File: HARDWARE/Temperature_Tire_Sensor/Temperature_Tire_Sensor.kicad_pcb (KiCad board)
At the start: 4 copper layers, 42 parts, among them IC1 MLX90621ESF-BAB-000-SP, J1 SWD_01x06, J2 CAN_01x04, SW1 RESET, U1 STM32L4P5RET6, U2 MIC5236, U3 MIC5306-2.6YD5-TR, U4 SN65HVD232, Y1 16MGHz

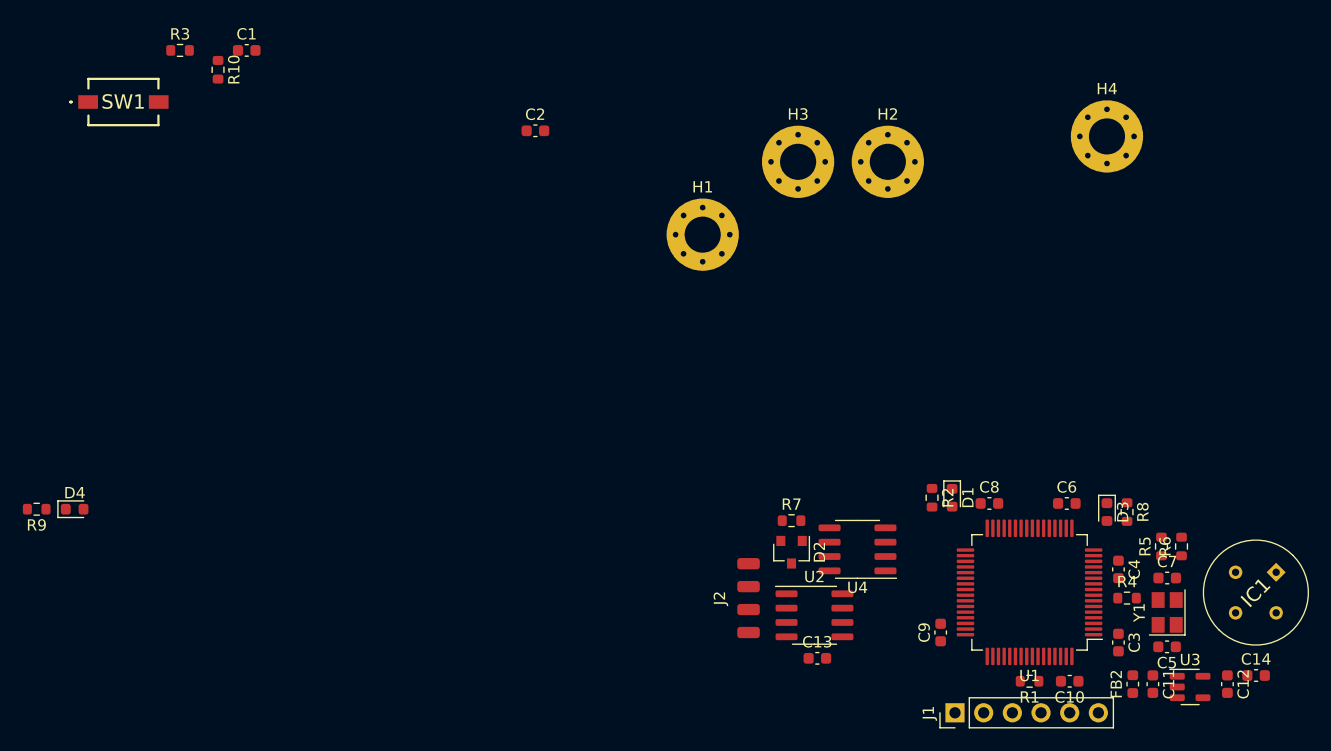
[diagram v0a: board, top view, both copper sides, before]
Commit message: pcb layout done - waiting for the confirmation of layout V1
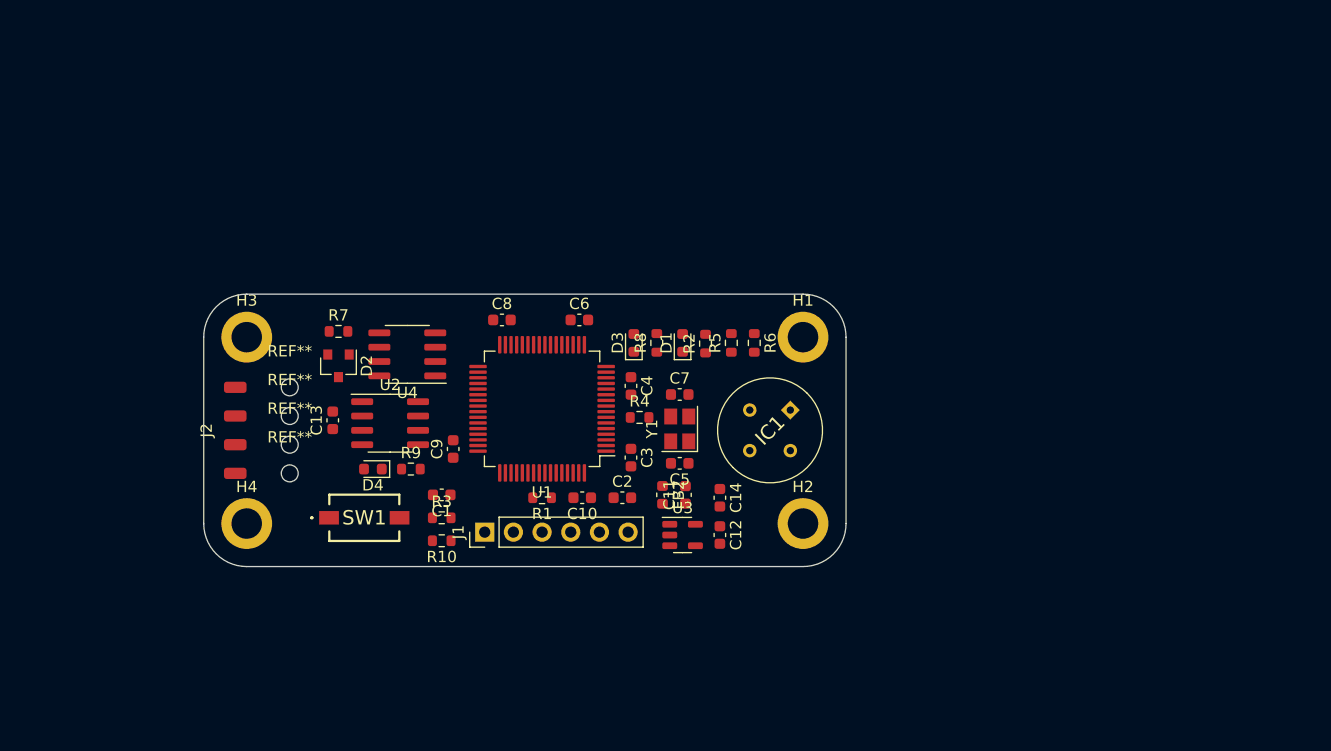
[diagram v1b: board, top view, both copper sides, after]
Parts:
- added REF**: MountingHole_2.1mm, MountingHole:MountingHole_2.1mm, F.Cu at (120.7, 111.1)
- added REF**: MountingHole_2.1mm, MountingHole:MountingHole_2.1mm, F.Cu at (120.7, 108.6)
- added REF**: MountingHole_2.1mm, MountingHole:MountingHole_2.1mm, F.Cu at (120.7, 116.2)
- added REF**: MountingHole_2.1mm, MountingHole:MountingHole_2.1mm, F.Cu at (120.7, 113.7)
- H1, H2, H3, H4: footprint MountingHole:MountingHole_3.2mm_M3_Pad_Via -> MountingHole:MountingHole_2.7mm_M2.5_ISO14580_Pad
- moved H4 83.6 mm to (116.8, 120.7)
- moved H3 51.2 mm to (116.8, 104.1)
- moved C14 50.0 mm to (158.8, 118.4), turned to -90 degrees
- moved J2 47.8 mm to (115.8, 112.4)
- moved C13 47.8 mm to (124.5, 111.5), turned to 90 degrees
- moved R3 47.4 mm to (134.1, 120.1)
- moved U3 46.9 mm to (155.4, 121.7)
- moved C12 46.9 mm to (158.8, 121.7)
- moved R10 46.2 mm to (134.1, 122.2), turned to 180 degrees
- moved C3 46.2 mm to (150.9, 114.8)
- moved C10 46.1 mm to (146.6, 118.4)
- moved C4 46.1 mm to (150.9, 108.5)
- moved C6 46.1 mm to (146.3, 102.6)
- moved C7 46.1 mm to (155.2, 109.2)
- moved C8 46.1 mm to (139.4, 102.6)
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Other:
- board outline added: 56.9 x 24.1 mm

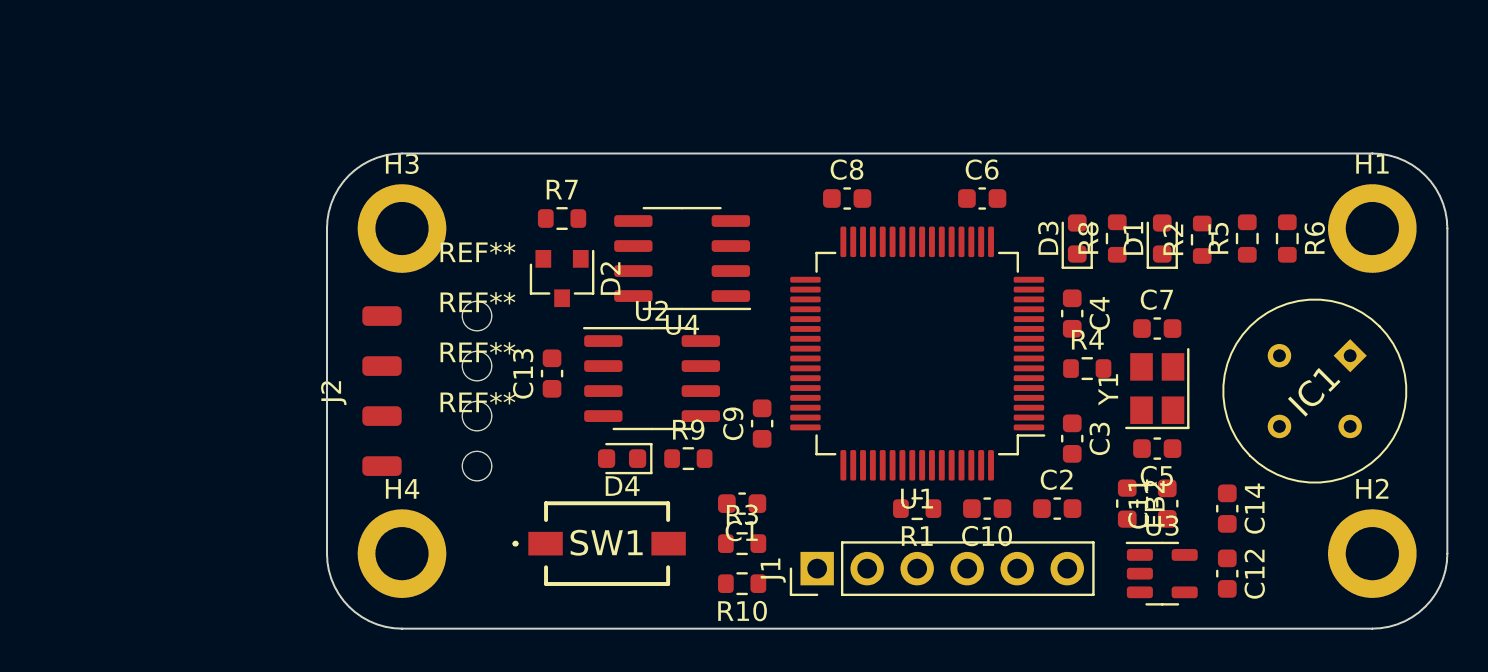
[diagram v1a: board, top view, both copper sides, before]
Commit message: Power planes has been added
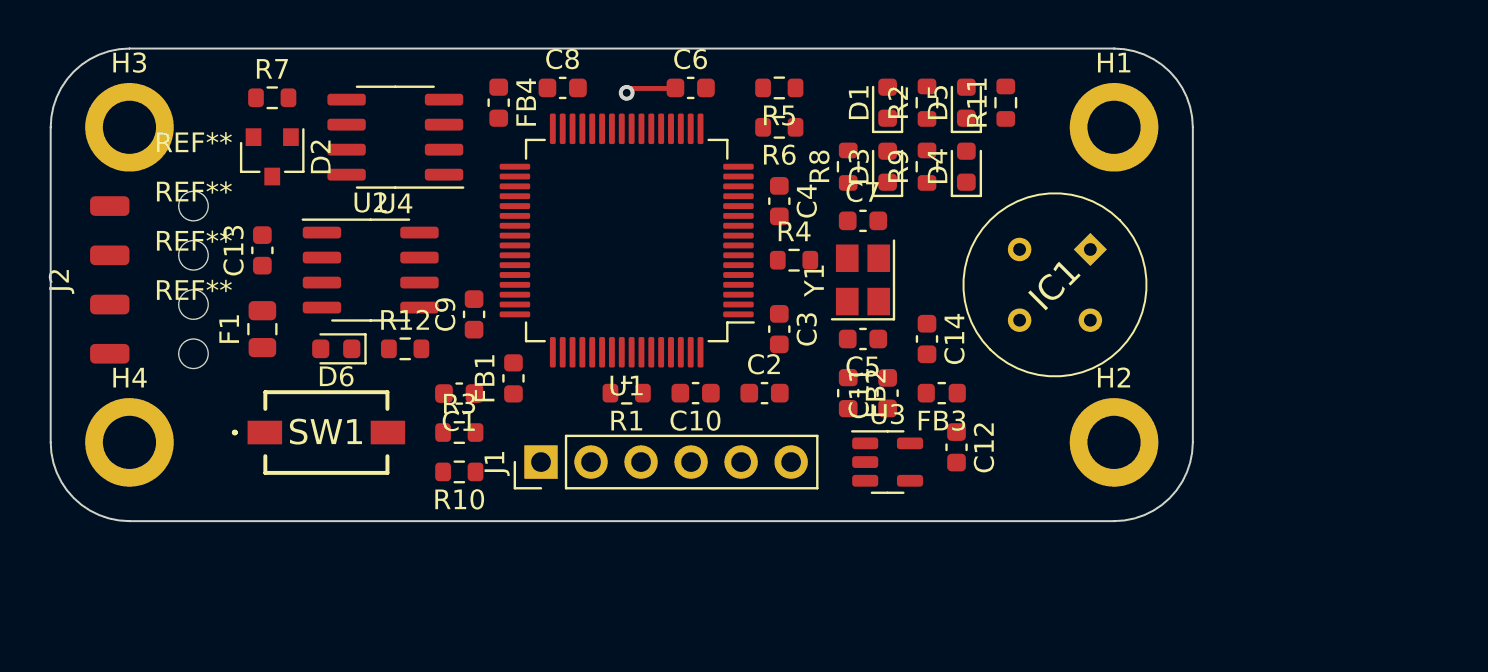
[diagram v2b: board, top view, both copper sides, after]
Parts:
- added D5: GREEN, Diode_SMD:D_0603_1608Metric, F.Cu at (145.5, 97.8)
- added D6: RED, Diode_SMD:D_0603_1608Metric, F.Cu at (113.5, 110.2)
- added F1: Polyfuse, Fuse:Fuse_0805_2012Metric, F.Cu at (109.8, 109.2)
- added FB1: 60R@100MHz, Inductor_SMD:L_0603_1608Metric, F.Cu at (122.5, 111.8)
- added FB3: 60R@100MHz, Inductor_SMD:L_0603_1608Metric, F.Cu at (144.2, 112.5)
- added FB4: 60R@100MHz, Inductor_SMD:L_0603_1608Metric, F.Cu at (121.8, 97.8)
- added R11: 1k5, Resistor_SMD:R_0603_1608Metric, F.Cu at (147.5, 97.8)
- added R12: 1k5, Resistor_SMD:R_0603_1608Metric, F.Cu at (117.0, 110.2)
- D1: value BLUE -> RED
- D3, D4: value RED -> YELLOW
- moved R6 26.4 mm to (136.0, 99.0), turned to 180 degrees
- moved R5 25.0 mm to (136.0, 97.0), turned to 180 degrees
- moved D4 22.9 mm to (145.5, 101.0), turned to 90 degrees
- moved R9 19.1 mm to (143.5, 101.0), turned to 90 degrees
- moved C14 17.5 mm to (143.5, 109.8)
- moved C13 16.0 mm to (109.8, 105.2)
- moved C2 16.0 mm to (135.2, 112.5)
- moved D2 16.0 mm to (110.2, 100.5)
- moved C5 15.9 mm to (140.2, 109.8)
- moved R7 15.9 mm to (110.2, 97.5)
- moved C4 15.9 mm to (136.0, 102.8)
- moved Y1 15.9 mm to (140.2, 106.8)
- moved C10 15.9 mm to (131.8, 112.5)
- moved C7 15.9 mm to (140.2, 103.8)
- moved C3 15.9 mm to (136.0, 109.2)
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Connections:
- C10 pad 1: +3V3 -> /+3V3_uC
- C14 pad 1: +2V6 -> Net-(C14-Pad1)
- C2 pad 1: +3V3 -> /+3V3_uC
- C3 pad 1: +3V3 -> /+3V3_uC
- C4 pad 1: +3V3 -> /+3V3_uC
- C6 pad 1: +3V3 -> /+3V3_uC
- C8 pad 1: +3V3 -> /+3V3_uC
- C9 pad 1: +3V3 -> /+3V3_uC
- D1 pad 2: /LED -> /LED_ERR
- D3 pad 2: /LED_ERR -> /LED_WAR1
- D4 pad 2: +3V3 -> /LED_WAR2
- IC1 pad 3: +2V6 -> Net-(C14-Pad1)
- U1 pad 1: +3V3 -> /+3V3_uC
- U1 pad 13: +3V3 -> /+3V3_uC
- U1 pad 16: unconnected-(U1-Pad16) -> /LED_WAR2
- U1 pad 19: +3V3 -> /+3V3_uC
- U1 pad 24: unconnected-(U1-Pad24) -> /LED_WAR1
- U1 pad 26: /LED -> /LED_OK
- U1 pad 32: +3V3 -> /+3V3_uC
- U1 pad 48: +3V3 -> /+3V3_uC
- U1 pad 64: +3V3 -> /+3V3_uC
- U2 pad 2: +24V -> Net-(F1-Pad2)
- U2 pad 4: +24V -> Net-(F1-Pad2)
- U4 pad 3: +3V3 -> Net-(FB4-Pad2)
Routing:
- net /+3V3_uC: track 0.00 -> 2.81 mm, vias 0 -> 1
- added copper zone on In2.Cu, net +3V3
- added copper zone on In2.Cu, net /+3V3_uC
- added copper zone on In1.Cu, net GND
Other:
- board size 56.9 x 24.1 mm -> 58 x 24 mm

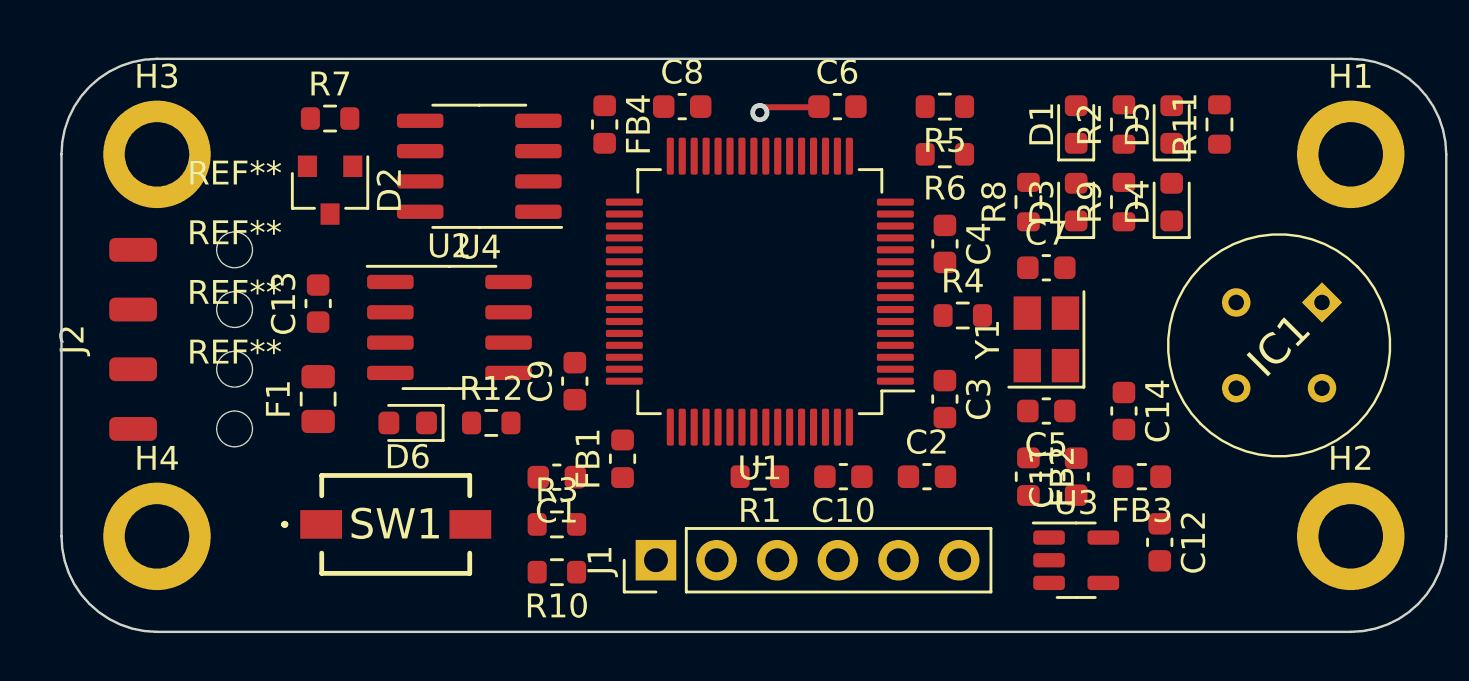
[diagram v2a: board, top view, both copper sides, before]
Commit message: Routing mostly done - GND and 3V3_uC vias have to be added
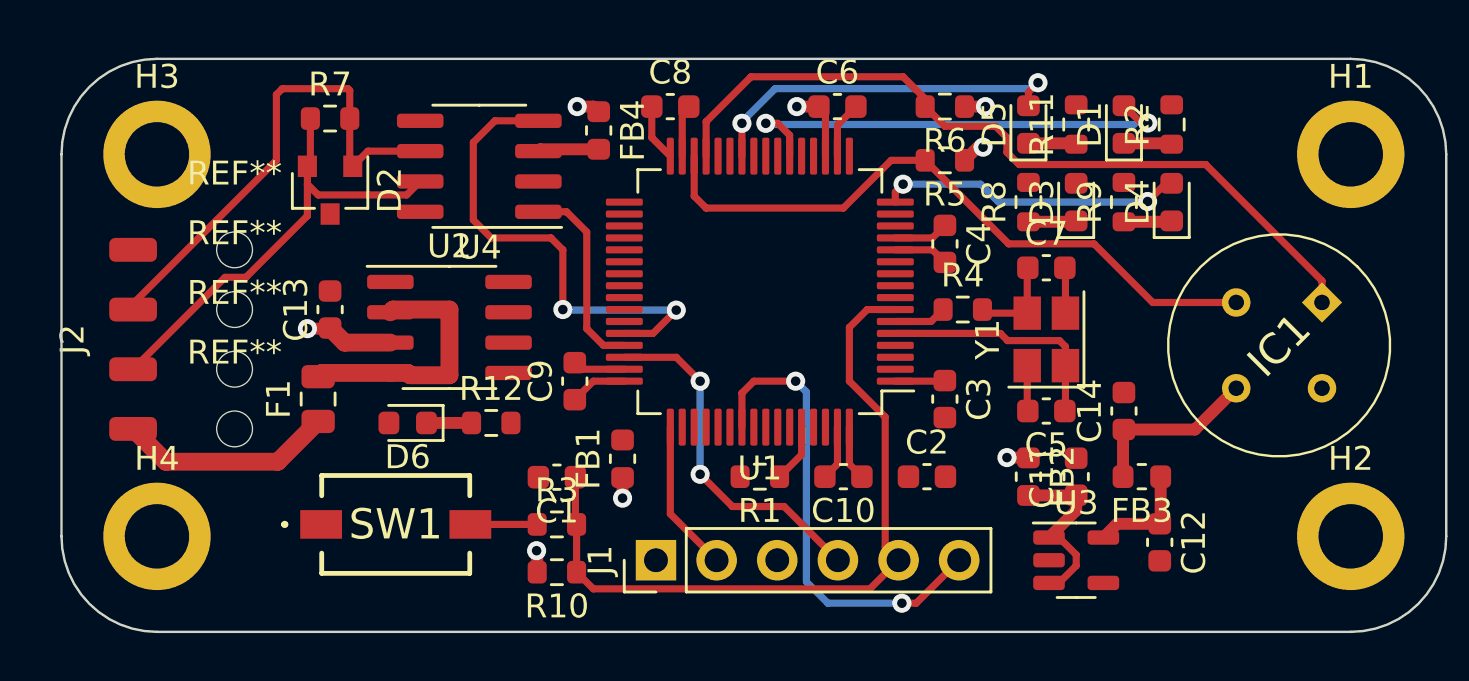
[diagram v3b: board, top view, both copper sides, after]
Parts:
- moved D5 6.00 mm to (139.5, 97.8)
- moved R11 6.00 mm to (141.5, 97.8)
- moved R5 2.25 mm to (136.0, 99.2)
- moved D1 2.00 mm to (143.5, 97.8)
- moved R2 2.00 mm to (145.5, 97.8)
- moved R6 2.00 mm to (136.0, 97.0)
- moved C13 0.56 mm to (110.2, 105.5)
- moved C8 0.50 mm to (124.5, 97.0)
- moved FB4 0.35 mm to (121.5, 98.0)
- moved R4 0.25 mm to (136.8, 105.5)
- turned C14 to 90 degrees
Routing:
- net /SCL: track 0.00 -> 33.1 mm
- net /NRST: track 0.00 -> 31.2 mm
- net /SDA: track 0.00 -> 27.9 mm
- net /CAN_L: track 0.00 -> 21.0 mm
- net /CAN_RX: track 0.00 -> 20.2 mm, vias 0 -> 2
- net /SWO: track 0.00 -> 20.0 mm, vias 0 -> 2
- net /CAN_H: track 0.00 -> 19.2 mm
- net /LED_ERR: track 0.00 -> 19.0 mm, vias 0 -> 2
- net /LED_OK: track 0.00 -> 15.6 mm, vias 0 -> 2
- net GND: track 0.00 -> 15.2 mm
- net /SWDIO: track 0.00 -> 14.8 mm, vias 0 -> 2
- net /LED_WAR2: track 0.00 -> 12.8 mm, vias 0 -> 2
- net /+3V3_uC: track 2.81 -> 14.9 mm
- net Net-(F1-Pad2): track 0.00 -> 10.9 mm
- net /OSC_IN: track 0.00 -> 10.1 mm
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
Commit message: Completed the routing
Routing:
- net GND: track 15.2 -> 45.9 mm, vias 0 -> 25
- net /LED_WAR1: track 0.00 -> 16.6 mm, vias 0 -> 2
- net /+3V3_uC: track 14.9 -> 21.5 mm, vias 1 -> 7
- net /NRST: track 31.2 -> 36.6 mm
- net /SWO: track 20.0 -> 15.8 mm, vias 2 -> 1
- net +3V3: track 9.28 -> 11.6 mm, vias 7 -> 9
- net /LED_OK: track 15.6 -> 17.8 mm
- net /LED_WAR2: track 12.8 -> 14.9 mm
- net Net-(C11-Pad1): track 7.58 -> 8.36 mm
- net /SWDIO: track 14.8 -> 14.6 mm, vias 2 -> 1

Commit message: A completed V1.0 of the board
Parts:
- added G***: LOGO, Logos:PUTM_LOGO_15mm, B.Cu at (128.0, 107.0)
- moved J2 0.25 mm to (102.0, 107.0)
- moved REF** 0.25 mm to (106.2, 105.8)
- moved REF** 0.25 mm to (106.2, 103.2)
- moved REF** 0.25 mm to (106.2, 110.8)
- moved REF** 0.25 mm to (106.2, 108.2)
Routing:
- net GND: track 45.9 -> 53.7 mm, vias 25 -> 32
- net +3V3: track 11.6 -> 10.2 mm, vias 9 -> 8
- net Net-(F1-Pad2): track 10.9 -> 9.66 mm
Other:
- board text added: "24V"
- board text added: "3V3"
- board text added: "CH"
- board text added: "CL"
- board text added: "CLK"
- board text added: "DIO"
- board text added: "GND"
- board text added: "Mateusz Koza"
- board text added: "NRST"
- board text added: "SWO"
- board text added: "TTS V1.0"
